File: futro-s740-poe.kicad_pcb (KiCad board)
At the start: 2 copper layers, 66 x 37 mm, 9 parts, among them J1 Conn_02x08, J2 Conn_02x08, U1 SM51589PEL, U2 AG5412

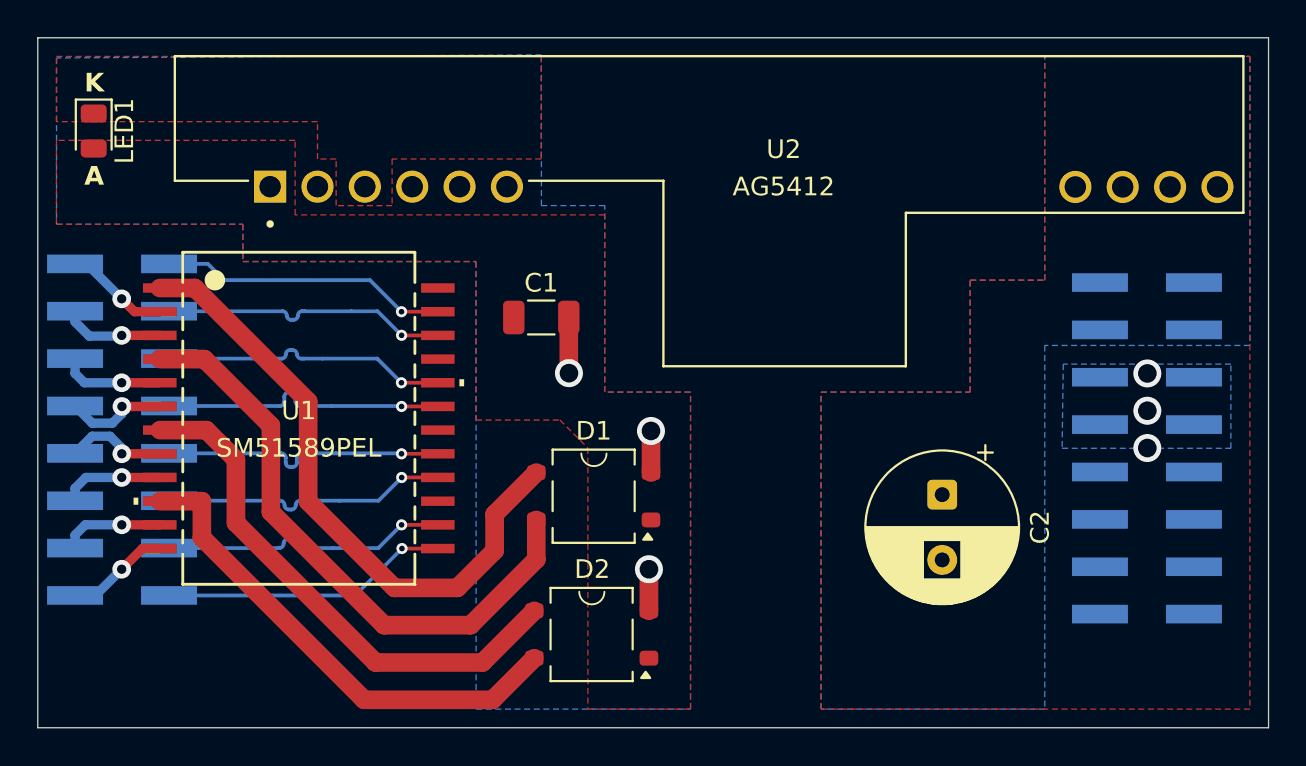
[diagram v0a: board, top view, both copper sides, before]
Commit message: fix cupper filled zone & via
Signed-off-by: Takuto Nagami <logica0419@gmail.com>
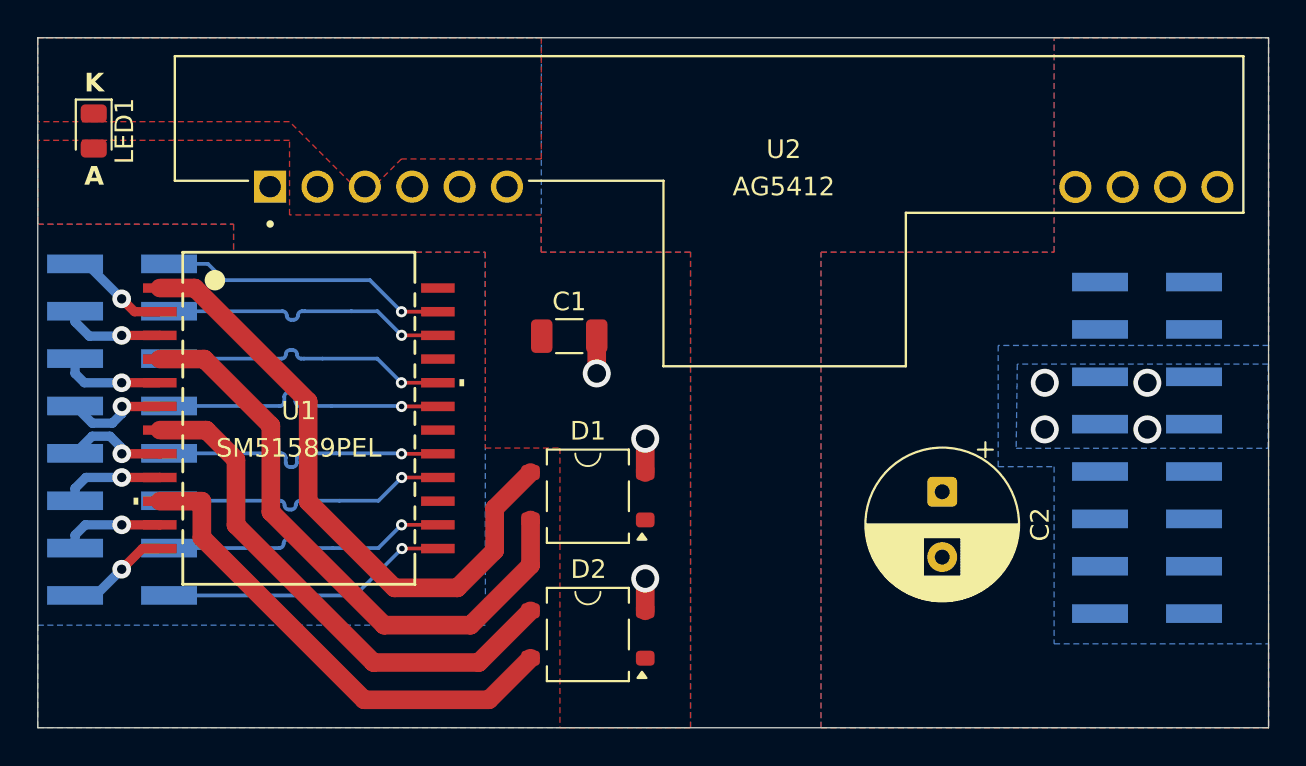
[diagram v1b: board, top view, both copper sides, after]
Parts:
- moved C1 1.80 mm to (66.5, 74.0)
- moved D1 0.31 mm to (67.5, 82.6)
- moved D2 0.20 mm to (67.5, 90.0)
- moved C2 0.15 mm to (86.5, 82.3)
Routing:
- net Net-(D1--): track 7.45 -> 5.54 mm
- net Net-(J2-Pin_5): vias 3 -> 4

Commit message: fix capacitor position
Signed-off-by: Takuto Nagami <logica0419@gmail.com>
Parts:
- moved C2 3.04 mm to (87.0, 79.3)
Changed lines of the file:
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@@
 		(capping no)
 		(filling no)
-		(zone_defaults)
 		(pcbplotparams
 			(layerselection 0x00000000_00000000_55555555_5755f5ff)
@@
 		(tags "LED")
 		(property "Reference" "LED1"
-			(at 0 -1.65 90)
+			(at 0 -2 90)
 			(layer "F.SilkS")
 			(effects
@@
 		(tags "SM51589PEL ")
 		(property "Reference" "U1"
-			(at 0 -0.405 0)
+			(at 0 -1.405 0)
 			(unlocked yes)
 			(layer "F.SilkS")
@@
 		)
 		(property "Value" "SM51589PEL"
-			(at 0 1.595 0)
+			(at 0 0.595 0)
 			(unlocked yes)
 			(layer "F.SilkS")
@@
 	(footprint "Capacitor_THT:CP_Radial_D8.0mm_P3.50mm"
 		(layer "F.Cu")
-		(at 86.5 82.347349 -90)
+		(at 87 79.347349 -90)
 		(descr "CP, Radial series, Radial, pin pitch=3.50mm, diameter=8mm, height=12mm, Electrolytic Capacitor")
 		(tags "CP Radial series Radial pin pitch 3.50mm diameter 8mm height 12mm Electrolytic Capacitor")
 		(property "Reference" "C2"
-			(at 1.75 -5.25 90)
-			(layer "F.SilkS")
-			(effects
+			(at 7.152651 0 180)
+			(layer "F.SilkS")
+			(effects
